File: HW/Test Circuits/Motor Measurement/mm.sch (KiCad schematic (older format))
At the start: 17 parts

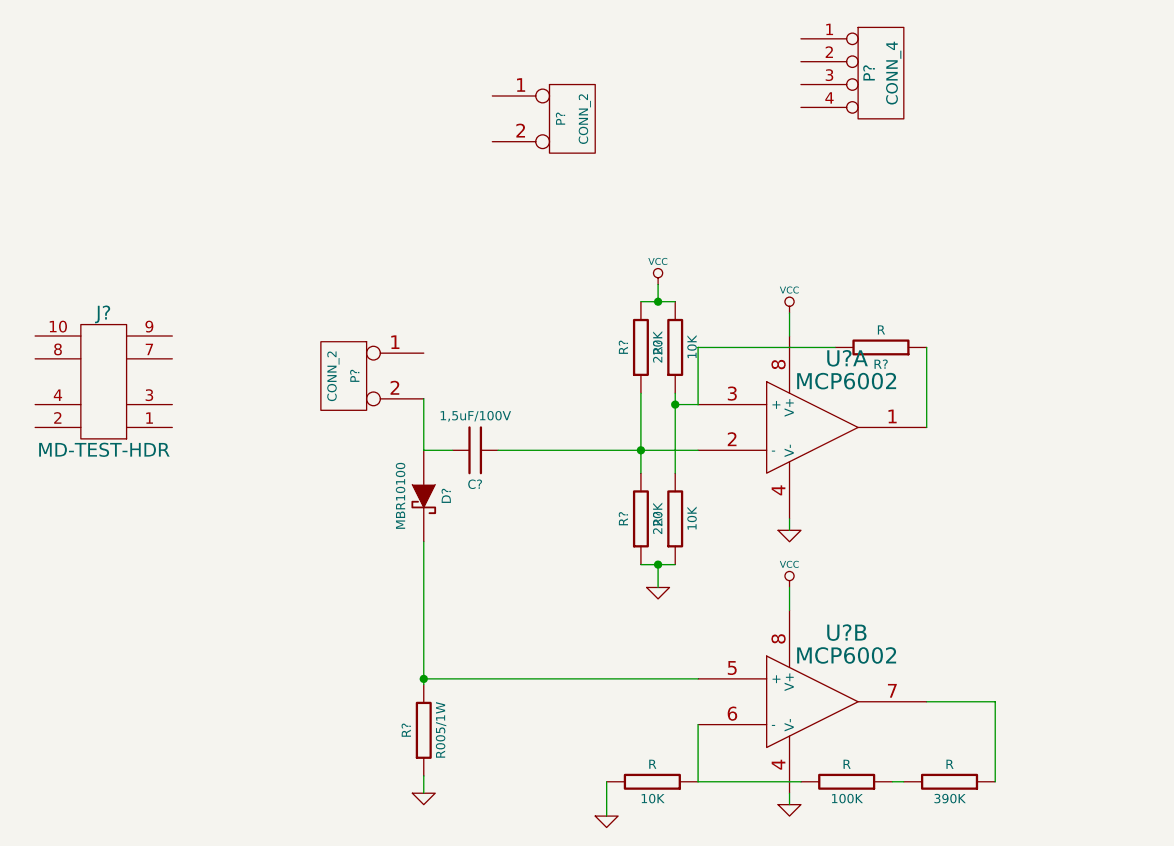
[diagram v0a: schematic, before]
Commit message: Motor Measurement Circuit added
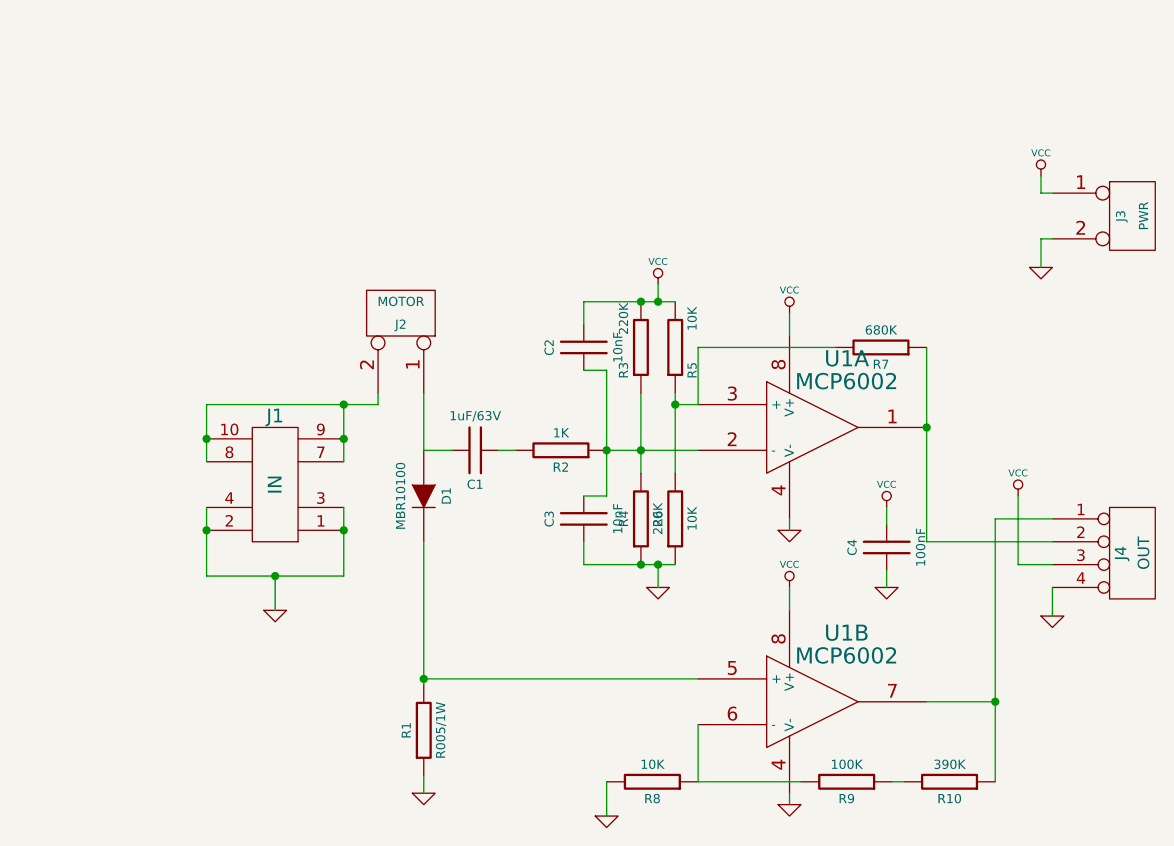
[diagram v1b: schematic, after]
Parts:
- removed D?: MBR10100, TO-220-2, symbol DIODESCH
- added C2, C3: 10nF, C2, symbol C
- added C4: 100nF, C1, symbol C
- added D1: MBR10100, TO220-2, symbol DIODE-HEXFRED
- added R2: 1K, R4, symbol R
- C1: renamed from C?; value 1,5uF/100V -> 1uF/63V; footprint ~ -> C2_3x1,75
- J1: renamed from J?; value MD-TEST-HDR -> IN; footprint ~ -> MD-TEST-HDR-F
- J2: renamed from P?; value CONN_2 -> MOTOR; footprint (none) -> MOLEX_36538_2
- J3: renamed from P?; value CONN_2 -> PWR; footprint (none) -> CONN_NCW254-02S
- J4: renamed from P?; value CONN_4 -> OUT; footprint (none) -> CONN_NCW254-04S
- R10: renamed from 390K; value R -> 390K; footprint ~ -> R4
- R7: renamed from R?; value R -> 680K; footprint ~ -> R4
- R8: renamed from 10K; value R -> 10K; footprint ~ -> R4
- R9: renamed from 100K; value R -> 100K; footprint ~ -> R4
- U1: renamed from U?; footprint ~ -> DIP-8
- gave numbers to parts that had none: 6
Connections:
- net GND: now also J1.1, J1.2, J1.3, J1.4, J3.2 (PM), J4.4 (P4), C3.2, C4.2
- net VCC: now also J3.1 (P1), J4.3 (P3), C2.1, C4.1
- net at R1.1, U1.5 (+): now also D1.1 (K)
- net at C1.1: now also J2.1 (P1), D1.3 (A); no longer J2.2 (PM)
- net at R3.2, R4.1, U1.2 (-): now also C2.2, C3.1, R2.2; no longer C1.2
- net at R7.2, U1.1: now also J4.2 (P2)
- net at R10.2, U1.7: now also J4.1 (P1)
- net at J1.10: now also J1.7, J1.8, J1.9, J2.2 (PM)
- new net: C1.2, R2.1
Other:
- moved on the sheet: J1, J2, J3, J4
